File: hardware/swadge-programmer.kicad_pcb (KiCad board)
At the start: 2 copper layers, 78.7 x 55.9 mm, 14 parts, among them J1 USB_B_Micro, SW1 SW_Push_SPDT, SW2 SW_Push_SPDT, SW3 SW_Push_SPDT, U1 BUS_PCIexpress, U2 CP2102N-A01-GQFN24

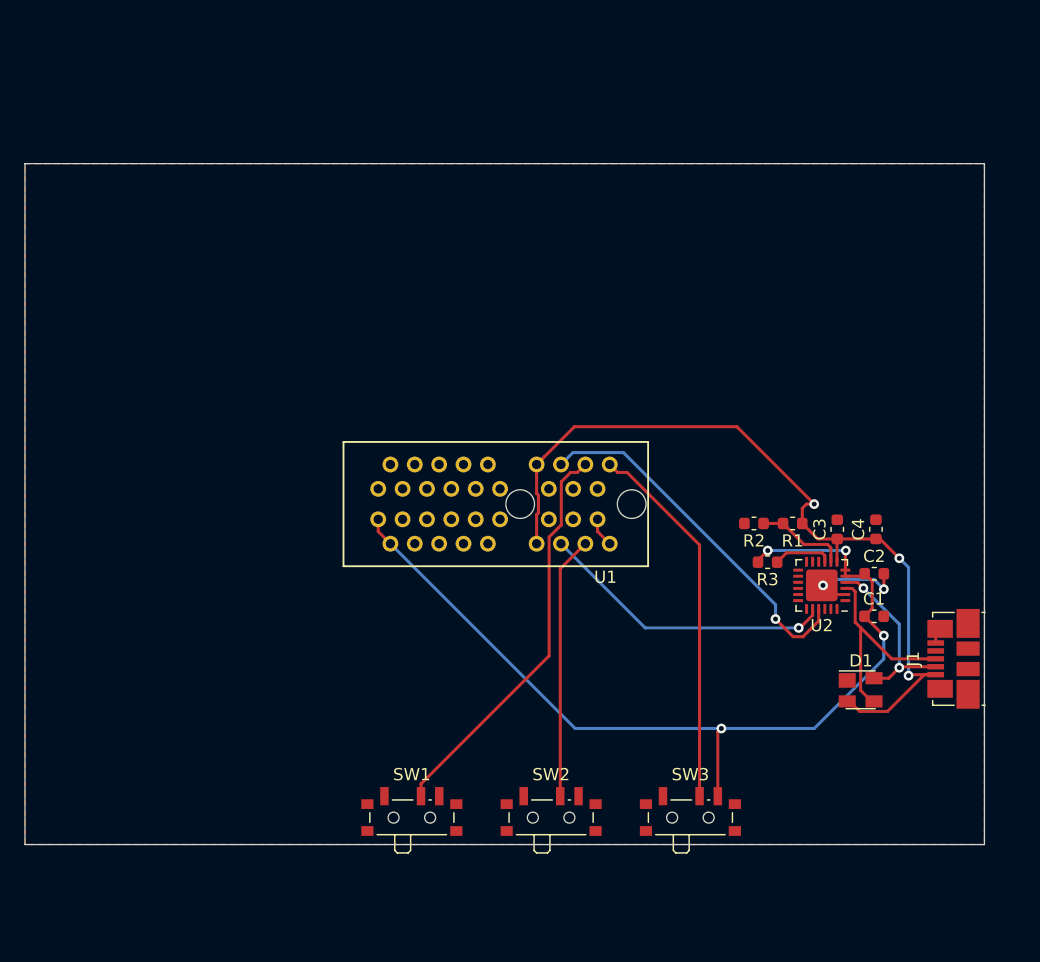
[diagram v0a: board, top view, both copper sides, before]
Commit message: Added power switches & pin headers to programmer
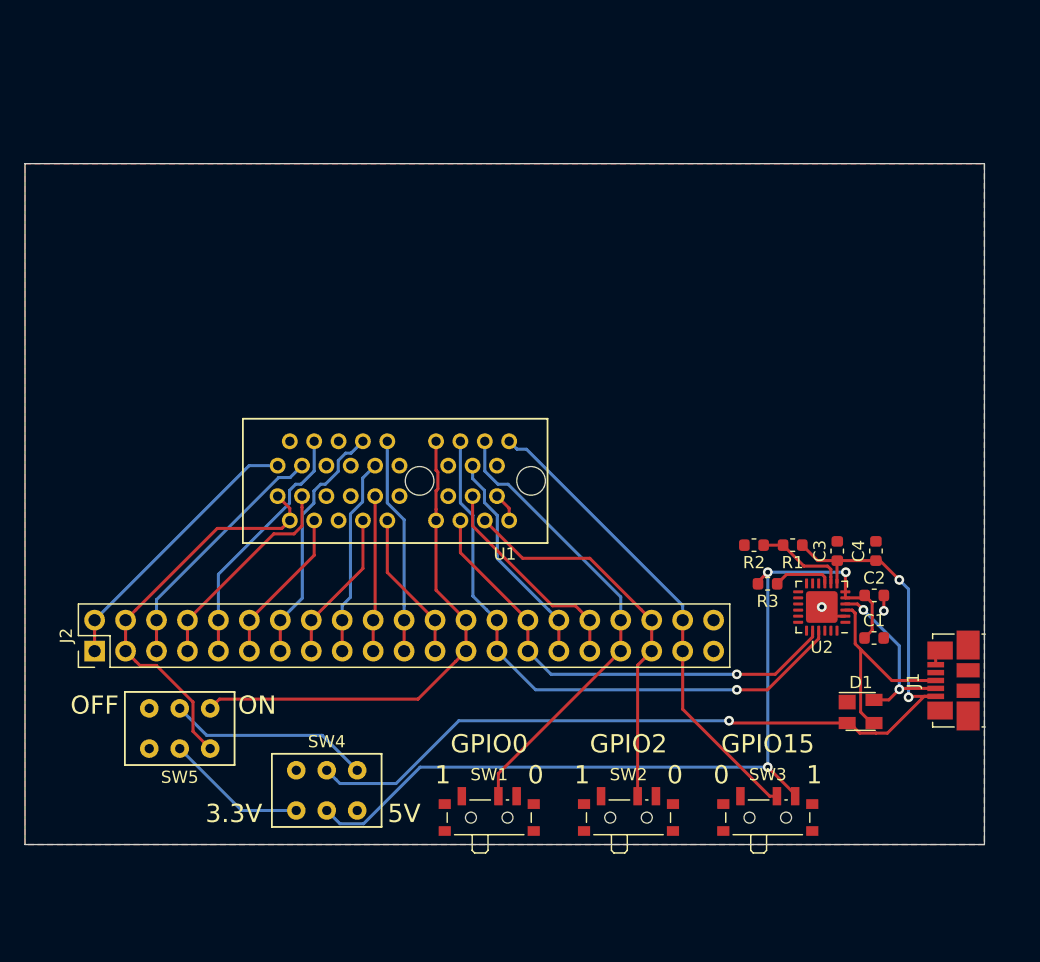
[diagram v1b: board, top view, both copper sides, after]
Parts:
- added J2: Conn_02x21_Top_Bottom, Connector_PinHeader_2.54mm:PinHeader_2x21_P2.54mm_Vertical, F.Cu at (107.3, 101.0)
- added SW4: SW_DPDT_x2, JS202011CQN:JS202011CQN, F.Cu at (126.4, 112.4)
- added SW5: SW_DPDT_x2, JS202011CQN:JS202011CQN, F.Cu at (114.3, 107.3)
- moved U1 8.47 mm to (134.0, 87.0)
- moved SW1 6.35 mm to (139.7, 114.3)
- moved SW2 6.35 mm to (151.1, 114.3)
- moved SW3 6.35 mm to (162.6, 114.3)
- moved C2 1.78 mm to (171.3, 96.4)
- moved D1 1.78 mm to (170.2, 105.9)
- moved J1 1.78 mm to (177.8, 103.4)
- moved R3 1.78 mm to (162.5, 95.4)
- moved U2 1.78 mm to (167.0, 97.3)
- moved C1 1.78 mm to (171.3, 99.9)
- moved C3 1.78 mm to (168.3, 92.8)
- moved C4 1.78 mm to (171.4, 92.8)
- moved R1 1.78 mm to (164.6, 92.3)
- moved R2 1.78 mm to (161.4, 92.3)
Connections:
- U1 pad A12: +5V -> 5V
- U1 pad B1: +3V3 -> 3.3V
- U1 pad B12: +5V -> 5V
- U1 pad B2: +3V3 -> 3.3V
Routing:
- net 5V: track 0.00 -> 41.3 mm
- net 3.3V: track 0.00 -> 33.5 mm
- net SW3: track 0.00 -> 22.8 mm
- net ADC_PIN: track 0.00 -> 20.7 mm
- net AUD_PWR: track 0.00 -> 20.7 mm
- net CS0: track 0.00 -> 20.5 mm
- net TX: track 30.0 -> 48.6 mm
- net SCL: track 0.00 -> 18.2 mm
- net SDA: track 0.00 -> 17.8 mm
- net MOSI: track 0.00 -> 17.8 mm
- net SW4: track 0.00 -> 17.6 mm
- net Net-(SW4-Pad6): track 0.00 -> 16.7 mm
- net SW5: track 0.00 -> 16.3 mm
- net RX: track 24.5 -> 39.0 mm
- net REST: track 0.00 -> 12.9 mm
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- added copper zone on B.Cu, net GND
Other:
- board text added: "0"
- board text added: "1"
- board text added: "3.3V"
- board text added: "5V"
- board text added: "GPIO0"
- board text added: "GPIO15"
- board text added: "GPIO2"
- board text added: "OFF"
- board text added: "ON"

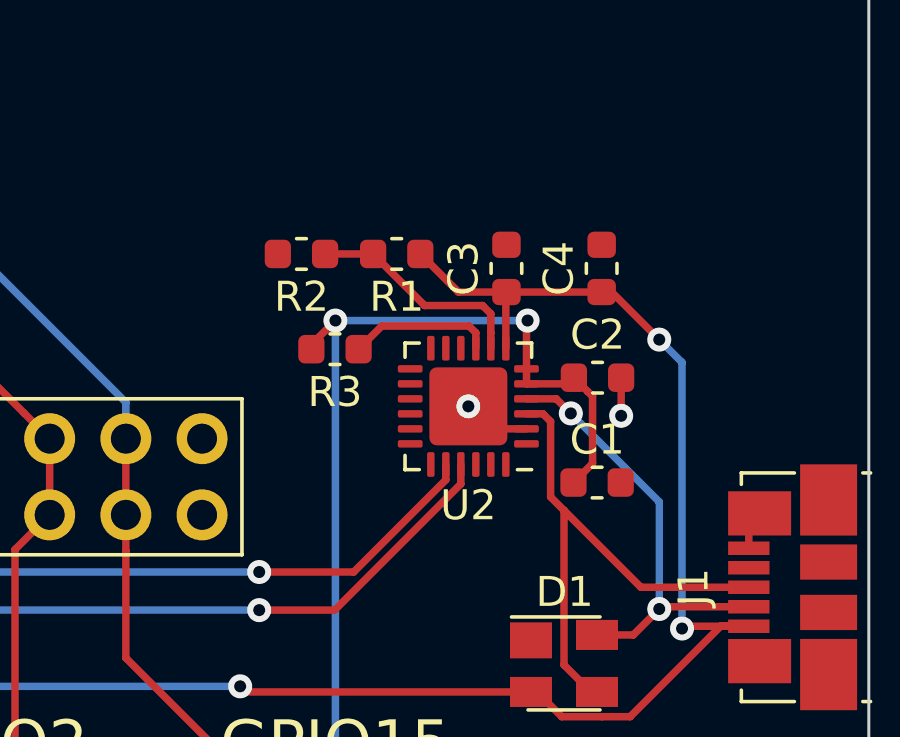
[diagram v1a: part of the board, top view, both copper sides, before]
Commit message: Started updating programmer to use local parts
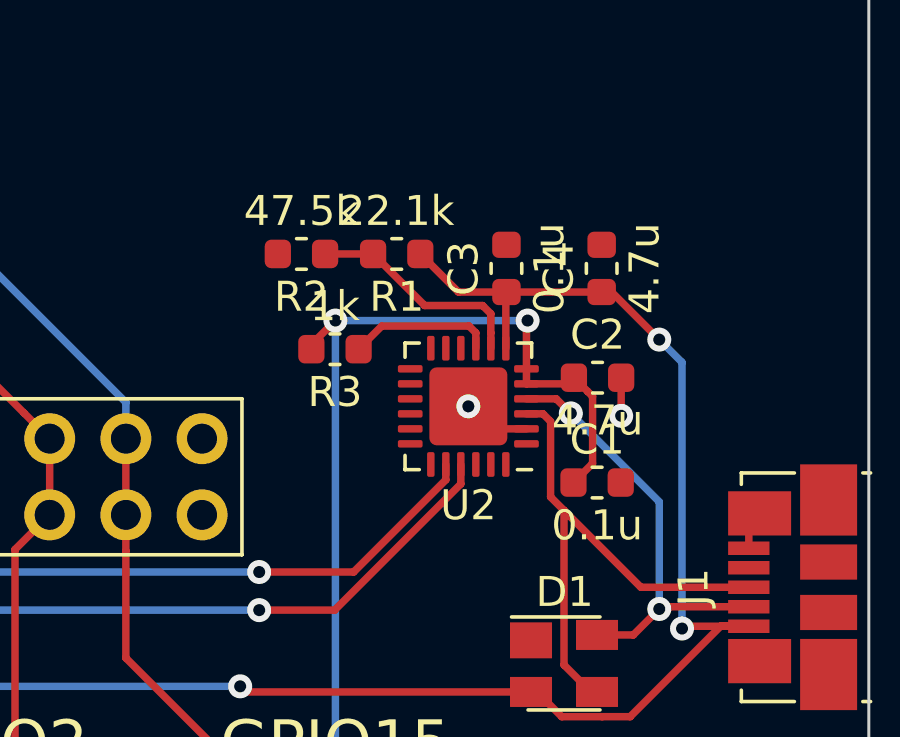
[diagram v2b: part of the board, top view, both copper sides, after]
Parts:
- C1, C2, C3, C4: footprint Capacitor_SMD:C_0603_1608Metric -> Swadge_Parts:C_0603_1608Metric
- J1: footprint Connector_USB:USB_Micro-B_Molex_47346-0001 -> Swadge_Parts:USB_Micro-B_Molex_47346-0001
- R1, R2, R3: footprint Resistor_SMD:R_0603_1608Metric -> Swadge_Parts:R_0603_1608Metric
- SW4, SW5: footprint JS202011CQN:JS202011CQN -> Swadge_Parts:JS202011CQN
- U1: footprint 10018784-10210TLF:10018784-10210TLF -> Swadge_Parts:10018784-10210TLF

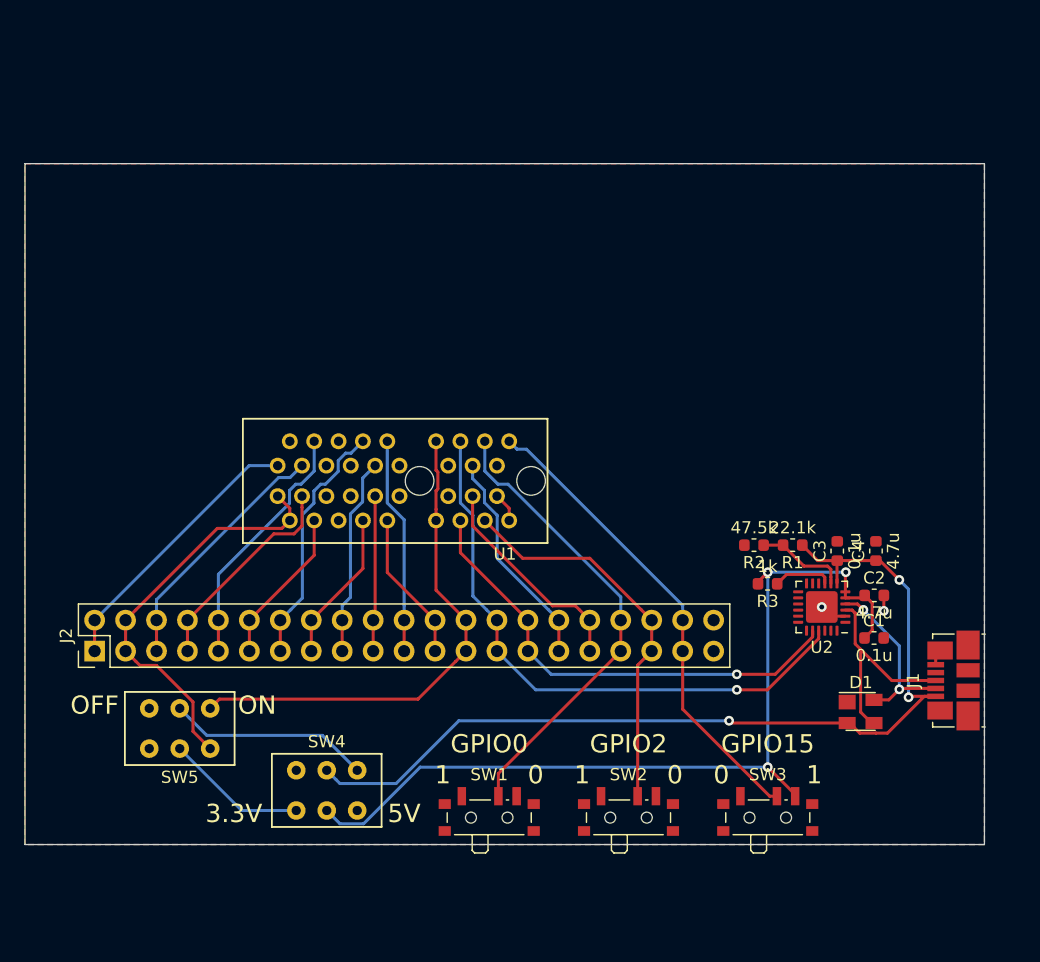
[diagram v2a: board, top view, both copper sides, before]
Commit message: Moved all programmer parts into this repo
Resized programmer, rerouted programmer, added holes
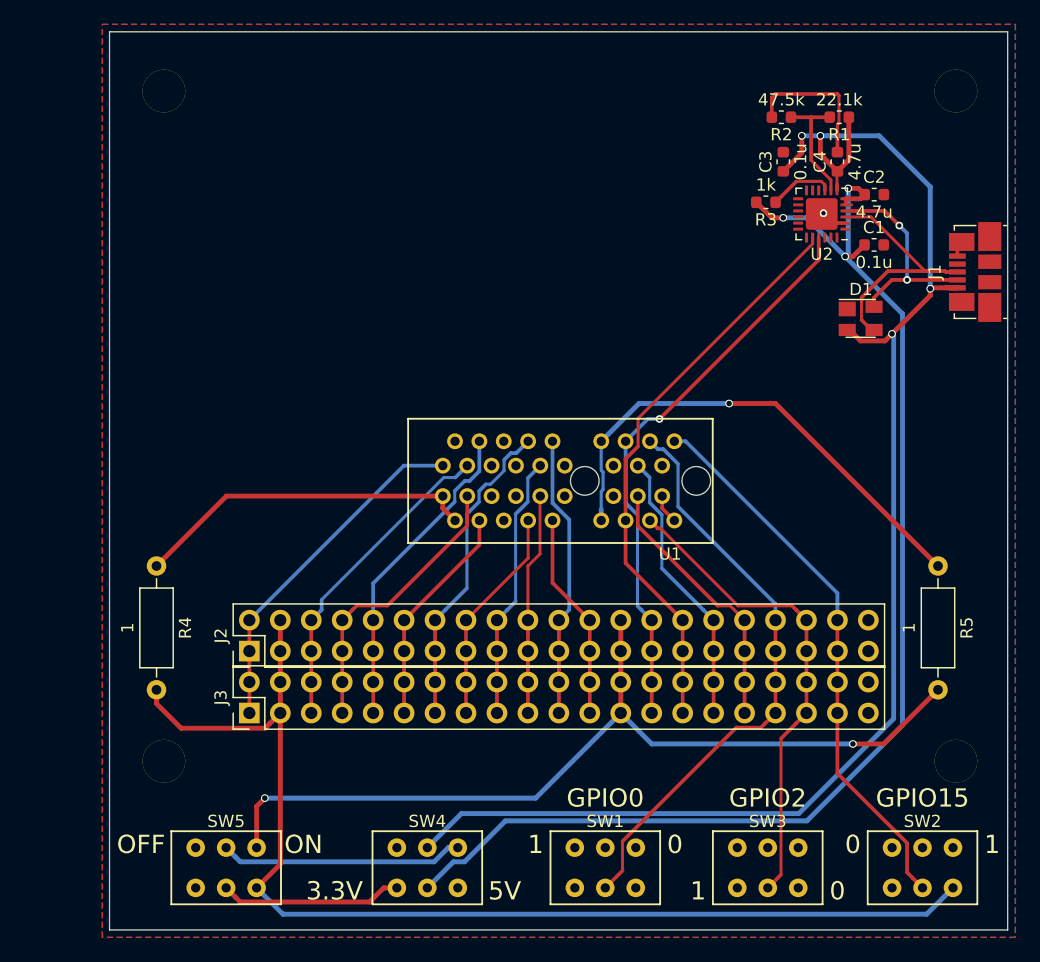
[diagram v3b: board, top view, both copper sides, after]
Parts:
- added H1: Hole, Swadge_Parts:Hole, F.Cu at (113.0, 55.0)
- added H2: Hole, Swadge_Parts:Hole, F.Cu at (113.0, 110.0)
- added H3: Hole, Swadge_Parts:Hole, F.Cu at (178.0, 55.0)
- added H4: Hole, Swadge_Parts:Hole, F.Cu at (178.0, 110.0)
- added J3: Conn_02x21_Top_Bottom, Swadge_Parts:PinHeader_2x21_P2.54mm_Vertical, F.Cu at (120.0, 106.0)
- added R4: 1, Swadge_Parts:R_Axial_DIN0207_L6.3mm_D2.5mm_P10.16mm_Horizontal, F.Cu at (112.4, 94.0)
- added R5: 1, Swadge_Parts:R_Axial_DIN0207_L6.3mm_D2.5mm_P10.16mm_Horizontal, F.Cu at (176.5, 94.0)
- D1: footprint Package_TO_SOT_SMD:SOT-143 -> Swadge_Parts:SOT-143
- J2: footprint Connector_PinHeader_2.54mm:PinHeader_2x21_P2.54mm_Vertical -> Swadge_Parts:PinHeader_2x21_P2.54mm_Vertical
- SW1, SW2, SW3: value SW_Push_SPDT -> SW_DPDT_x2; footprint Button_Switch_SMD:SW_SPDT_PCM12 -> Swadge_Parts:JS202011CQN
- U2: footprint Package_DFN_QFN:QFN-24-1EP_4x4mm_P0.5mm_EP2.6x2.6mm -> Swadge_Parts:QFN-24-1EP_4x4mm_P0.5mm_EP2.6x2.6mm
- moved R1 35.3 mm to (168.4, 57.1)
- moved R2 35.2 mm to (163.7, 57.1)
- moved J1 33.6 mm to (179.6, 69.8)
- moved C2 32.9 mm to (171.3, 63.5)
- moved D1 32.3 mm to (170.2, 73.7)
- moved U2 32.3 mm to (167.0, 65.1)
- moved C1 32.3 mm to (171.3, 67.6)
- moved C3 32.2 mm to (163.8, 60.8)
- moved C4 32.1 mm to (168.3, 60.8)
- moved R3 31.3 mm to (162.4, 64.1)
- moved SW2 24.5 mm to (175.3, 118.7)
- moved U1 13.6 mm to (147.5, 87.0)
- moved J2 12.7 mm to (120.0, 101.0)
- moved SW5 12.0 mm to (118.1, 118.7)
- moved SW1 10.5 mm to (149.2, 118.7)
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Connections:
- J1 pad 4: Net-(J1-Pad4) -> (no net)
- SW1 pad 1: Net-(SW1-Pad1) -> (no net)
- SW2 pad 1: Net-(SW2-Pad1) -> (no net)
- SW2 pad 2: GPIO2 -> GPIO15
- SW2 pad 3: GND -> 3.3V
- SW3 pad 1: Net-(SW3-Pad1) -> (no net)
- SW3 pad 2: GPIO15 -> GPIO2
- SW3 pad 3: +3V3 -> GND
- SW4 pad 3: Net-(SW4-Pad3) -> (no net)
- SW4 pad 4: Net-(SW4-Pad4) -> (no net)
- SW5 pad 3: Net-(SW5-Pad3) -> (no net)
- SW5 pad 6: Net-(SW5-Pad6) -> (no net)
- U1 pad A11: Net-(U1-PadA11) -> (no net)
- U1 pad A12: 5V -> Net-(R5-Pad1)
- U1 pad A13: Net-(U1-PadA13) -> (no net)
- U1 pad A17: Net-(U1-PadA17) -> (no net)
- U1 pad A2: Net-(U1-PadA2) -> (no net)
- U1 pad A5: Net-(U1-PadA5) -> (no net)
- U1 pad A6: Net-(U1-PadA6) -> (no net)
- U1 pad A7: Net-(U1-PadA7) -> (no net)
- U1 pad B1: 3.3V -> Net-(R4-Pad1)
- U1 pad B11: Net-(U1-PadB11) -> (no net)
- U1 pad B12: 5V -> Net-(R5-Pad1)
- U1 pad B13: Net-(U1-PadB13) -> (no net)
- U1 pad B2: 3.3V -> Net-(R4-Pad1)
- U1 pad B5: Net-(U1-PadB5) -> (no net)
- U1 pad B6: Net-(U1-PadB6) -> (no net)
- U1 pad B7: Net-(U1-PadB7) -> (no net)
- U2 pad 1: Net-(U2-Pad1) -> (no net)
- U2 pad 10: Net-(U2-Pad10) -> (no net)
- U2 pad 11: Net-(U2-Pad11) -> (no net)
- U2 pad 12: Net-(U2-Pad12) -> (no net)
- U2 pad 13: Net-(U2-Pad13) -> (no net)
- U2 pad 14: Net-(U2-Pad14) -> (no net)
- U2 pad 15: Net-(U2-Pad15) -> (no net)
- U2 pad 16: Net-(U2-Pad16) -> (no net)
- U2 pad 17: Net-(U2-Pad17) -> (no net)
- U2 pad 18: Net-(U2-Pad18) -> (no net)
- U2 pad 19: Net-(U2-Pad19) -> (no net)
- U2 pad 22: Net-(U2-Pad22) -> (no net)
- U2 pad 23: Net-(U2-Pad23) -> (no net)
- U2 pad 24: Net-(U2-Pad24) -> (no net)
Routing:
- net 3.3V: track 33.5 -> 94.4 mm
- net +5V: track 77.4 -> 121.3 mm, vias 3 -> 4
- net Net-(R5-Pad1): track 0.00 -> 41.1 mm, vias 0 -> 1
- net +3V3: track 73.8 -> 106.0 mm
- net 5V: track 41.3 -> 73.0 mm, vias 0 -> 2
- net Net-(R4-Pad1): track 0.00 -> 28.3 mm
- net GND: track 7.24 -> 19.5 mm, vias 2 -> 1
- net GPIO0: track 38.4 -> 48.2 mm
- net RX: track 39.0 -> 47.3 mm, vias 1 -> 0
- net GPIO2: track 32.0 -> 39.5 mm
- net GPIO15: track 39.0 -> 45.6 mm
- net SW3: track 22.8 -> 28.7 mm
- net SW4: track 17.6 -> 23.5 mm
- net SW2: track 12.8 -> 18.2 mm
- net AUD_PWR: track 20.7 -> 26.2 mm
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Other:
- board size 78.7 x 55.9 mm -> 73.7 x 73.7 mm
- net class Default: clearance 0.2 -> 0.19558; trace_width 0.25 -> 0.3048; via_dia 0.8 -> 0.635; via_drill 0.4 -> 0.3556
- net class Power added: clearance 0.19558, trace_width 0.4, via_dia 0.635, via_drill 0.45
- rule trace_clearance: 0.2 -> 0.19558

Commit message: Updated programmer traces, parts, BOM
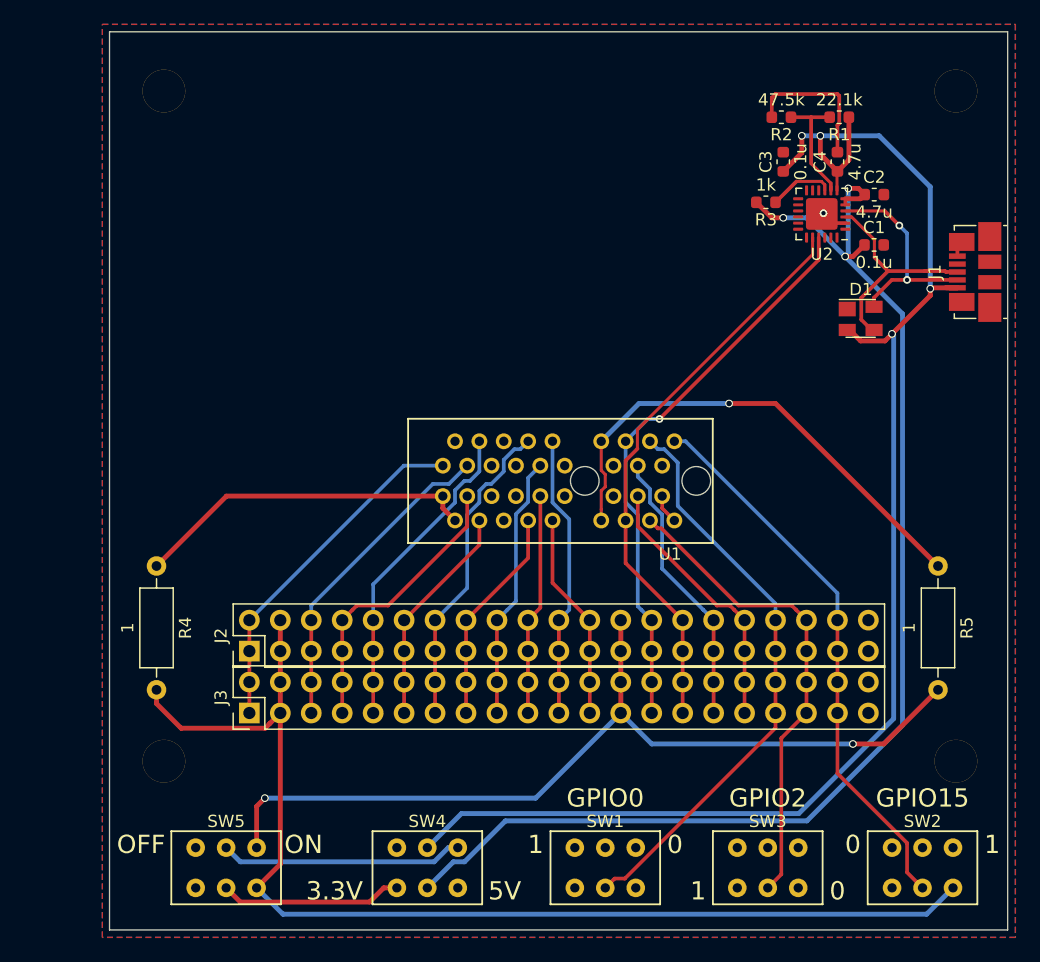
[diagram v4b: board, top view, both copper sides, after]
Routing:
- net Net-(D1-Pad3): track 20.8 -> 18.6 mm
- net GND: track 19.5 -> 17.9 mm
- net GPIO0: track 48.2 -> 47.5 mm
- net +3V3: track 106.0 -> 105.5 mm
